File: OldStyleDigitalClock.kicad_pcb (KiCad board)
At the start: 2 copper layers, 175 x 85 mm, 89 parts, among them J1 USB_A_OUT, J2 USB_A_OUT, J3 USB_C_IN, SW1 Set minutes, SW2 Set hours, U1 4071, U10 CD4026BE, U11 NE555D, U12 CD4060BE, U13 CD4017BE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

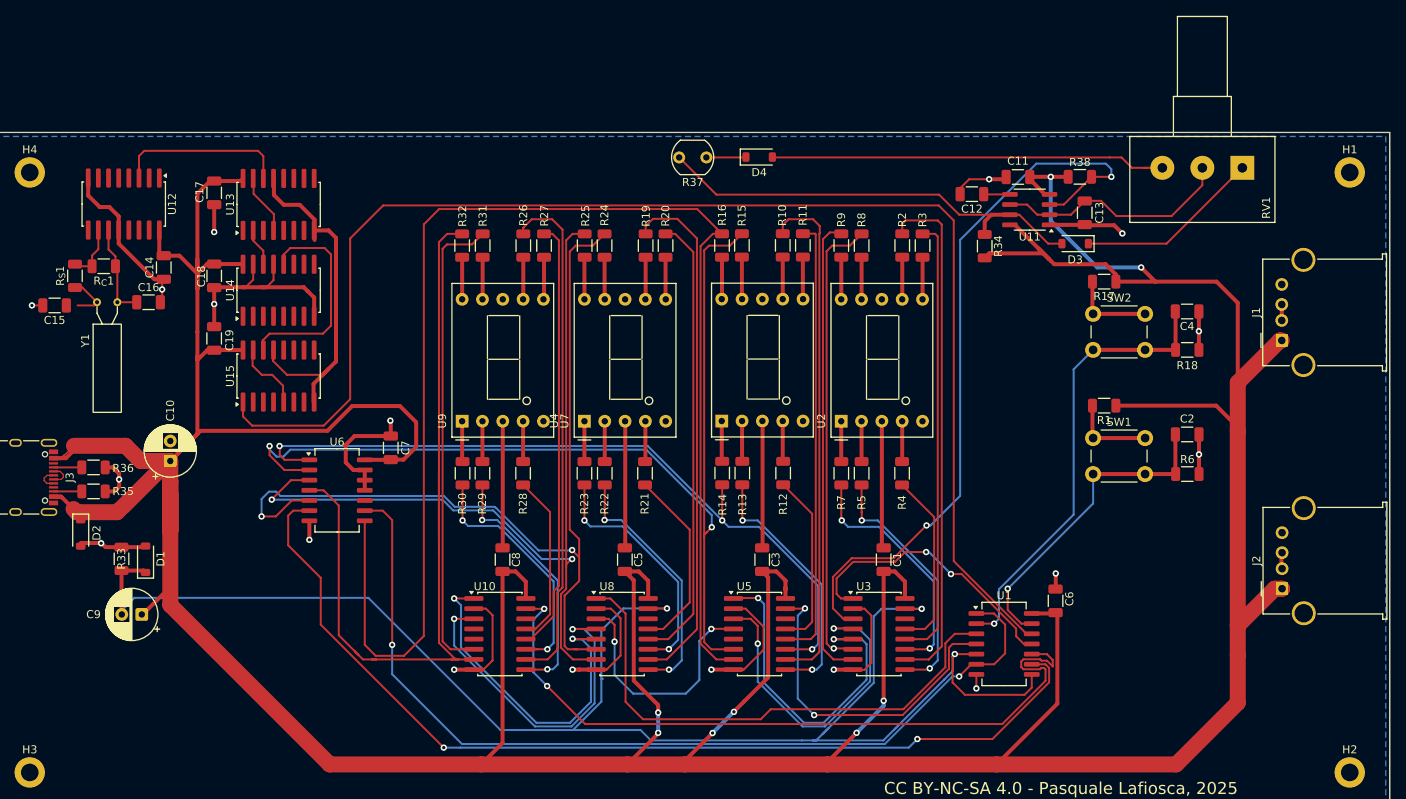
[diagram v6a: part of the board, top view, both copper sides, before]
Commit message: Checked DRC, all ok except USB C clearances
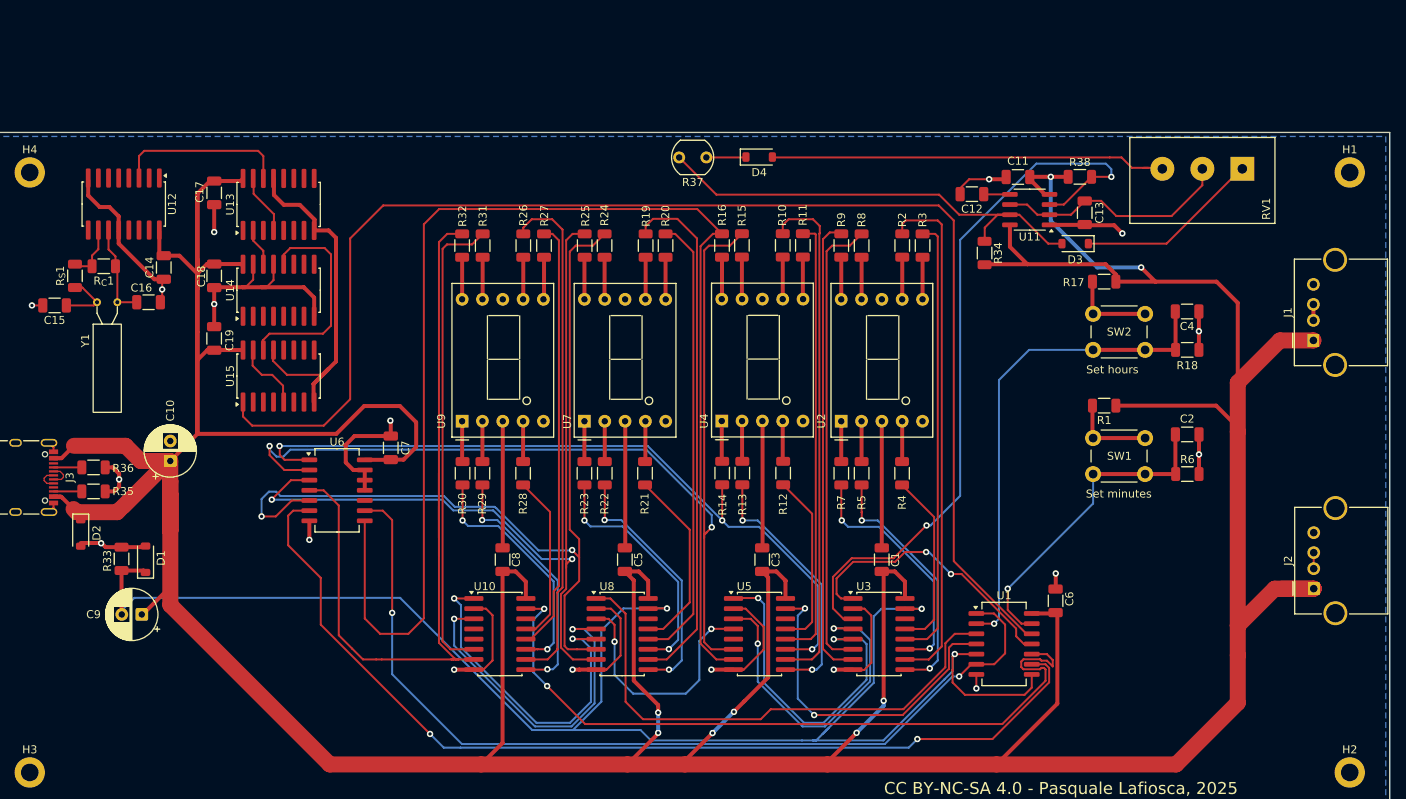
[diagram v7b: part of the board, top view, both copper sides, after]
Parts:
- moved J1 3.96 mm to (190.5, 51.0)
- moved J2 3.96 mm to (190.5, 82.0)
- moved R34 0.86 mm to (149.3, 40.1)
- moved C1 0.24 mm to (136.5, 78.4)
- moved RV1 0.12 mm to (181.6, 29.6)
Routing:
- net +5V: track 649.5 -> 681.2 mm
- net Net-(U5-G): track 173.2 -> 167.7 mm
- net Net-(C4-Pad2): track 56.8 -> 61.5 mm
- net GND: track 282.7 -> 286.5 mm
- net Net-(U5-E): track 97.4 -> 98.9 mm
- net Net-(C15-Pad1): track 6.12 -> 7.52 mm
- net Net-(U10-G): track 129.7 -> 128.4 mm
- net MR: track 200.7 -> 199.5 mm
- net Net-(U3-F): vias 1 -> 0

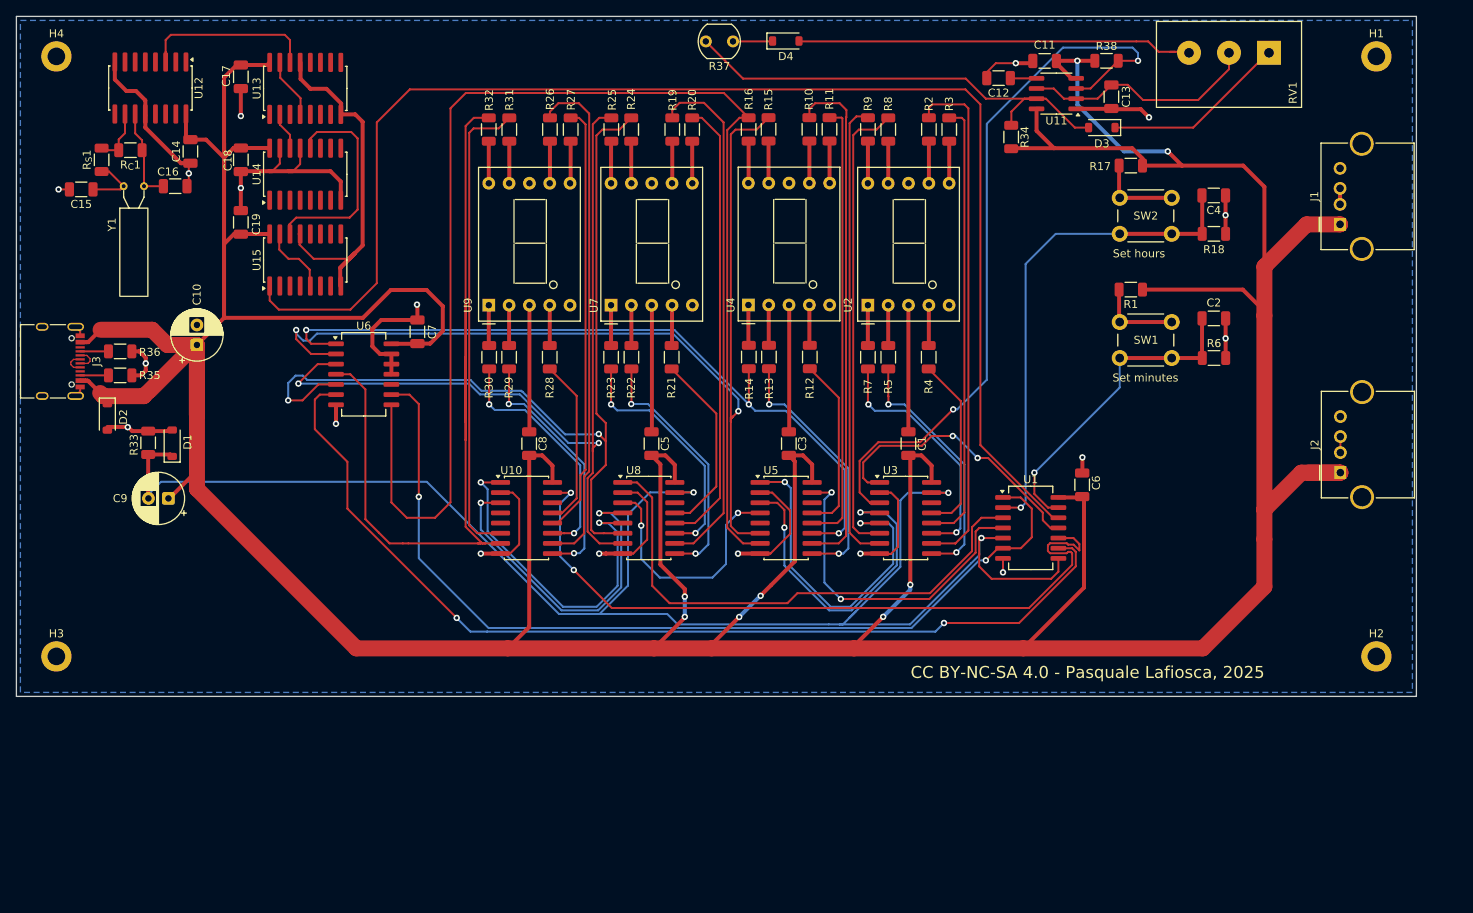
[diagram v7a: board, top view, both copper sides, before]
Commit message: Reduced board size, RDC passing except for USB C clearance.
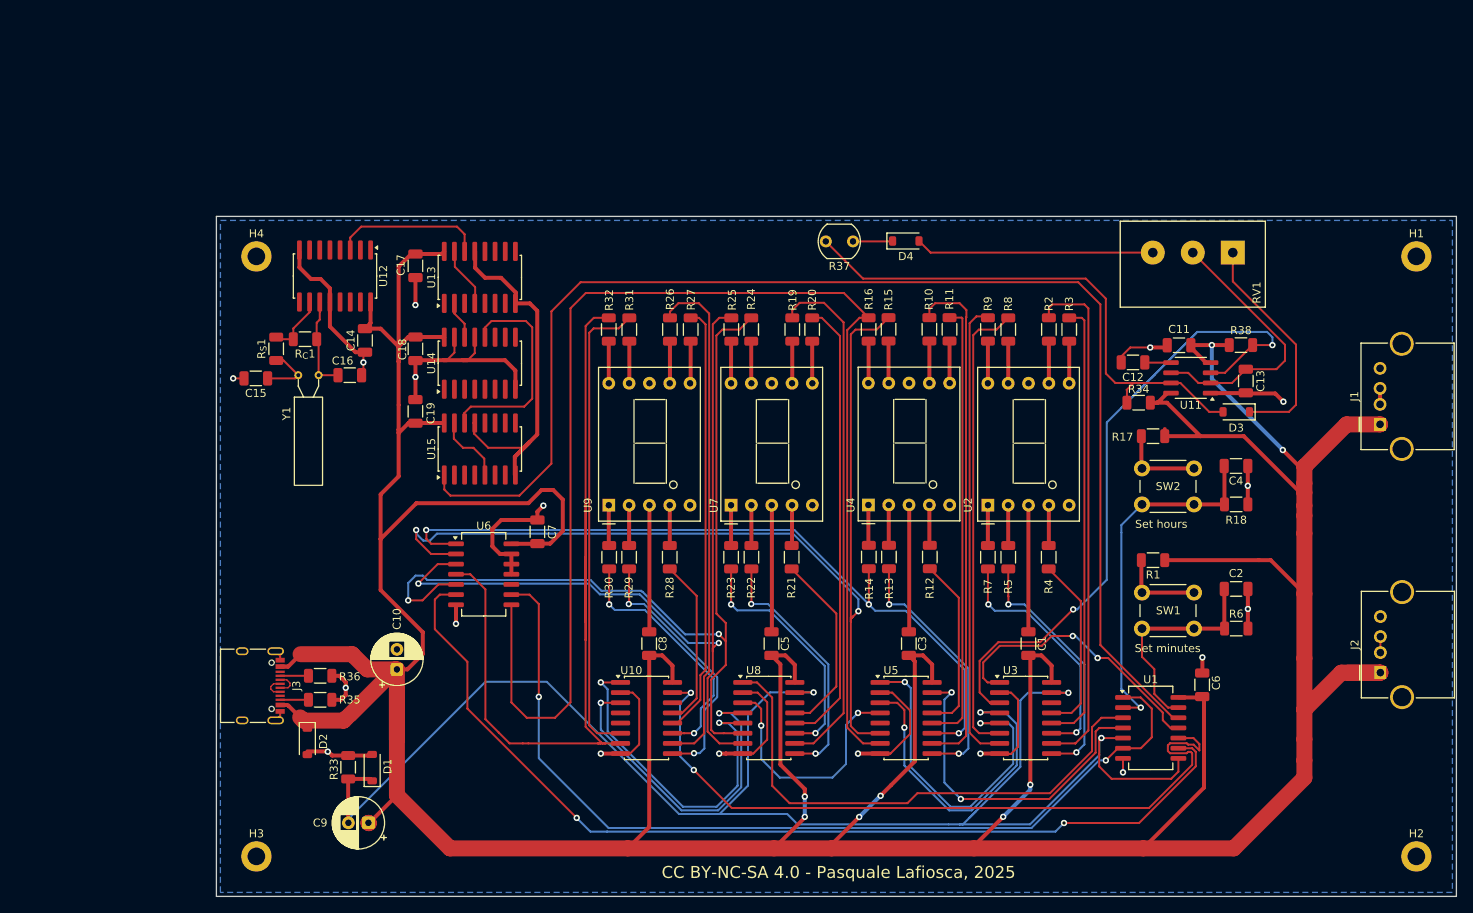
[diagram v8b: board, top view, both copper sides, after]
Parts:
- moved C10 47.6 mm to (72.6, 106.6)
- moved C9 47.6 mm to (69.0, 125.8)
- moved D1 47.6 mm to (69.5, 118.9)
- moved D2 47.6 mm to (61.4, 115.6)
- moved R33 47.6 mm to (66.5, 118.9)
- moved R35 47.6 mm to (63.0, 110.4)
- moved R36 47.6 mm to (63.0, 107.4)
- moved J3 47.6 mm to (54.3, 108.7)
- moved C13 39.3 mm to (178.7, 70.6)
- moved U11 39.3 mm to (171.8, 70.2)
- moved R38 39.3 mm to (178.1, 66.1)
- moved C11 39.3 mm to (170.3, 66.1)
- moved C12 39.3 mm to (164.6, 68.2)
- moved D3 39.3 mm to (177.5, 74.4)
- moved R34 36.8 mm to (165.3, 73.3), turned to 180 degrees
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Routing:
- net +5V: track 681.2 -> 618.9 mm
- net Net-(D4-A): track 50.0 -> 29.8 mm
- net Net-(C4-Pad2): track 61.5 -> 44.9 mm
- net Net-(C2-Pad2): track 40.4 -> 27.8 mm, vias 1 -> 0
- net Net-(D3-A): track 57.9 -> 67.4 mm
- net 1_MIN_CLK: track 171.2 -> 163.6 mm
- net Net-(D3-K): track 23.1 -> 28.5 mm
- net Net-(U11-THR): track 29.7 -> 34.2 mm
- net /Time/CLK 2 Hz: track 23.1 -> 19.0 mm
- net LED_PWM: track 92.3 -> 96.4 mm
- net MR: track 199.5 -> 196.0 mm
- net Net-(U10-E): track 30.5 -> 31.8 mm
- net Net-(U10-D): track 31.7 -> 33.1 mm
- net Net-(U12-(PHI)I): track 11.7 -> 12.7 mm
- net GND: track 286.5 -> 285.6 mm
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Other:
- board size 175 x 85 mm -> 155 x 85 mm
